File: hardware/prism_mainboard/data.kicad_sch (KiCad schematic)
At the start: 0 parts

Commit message: Mainboard Updates
Started a lot of the basic schematic nets like GND and Power nets. Major Change: Decided on using the XC7Z015-1CLG485I instead of the 7010 or 7020 due to the ability to use HDMI interfaces with an adapter and more LUTs. Updated schematic symbols and footprints accordingly. Added Memory, Encoder, MicroSD schematics. Added LimeSDR footprints as well. Will Try to add Power to the entire board next.
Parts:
- added IC1, IC2: KTDM2G3C618BGCEAT, BGA96C80P9X16_750X1300X100, symbol SamacSys:KTDM2G3C618BGCEAT

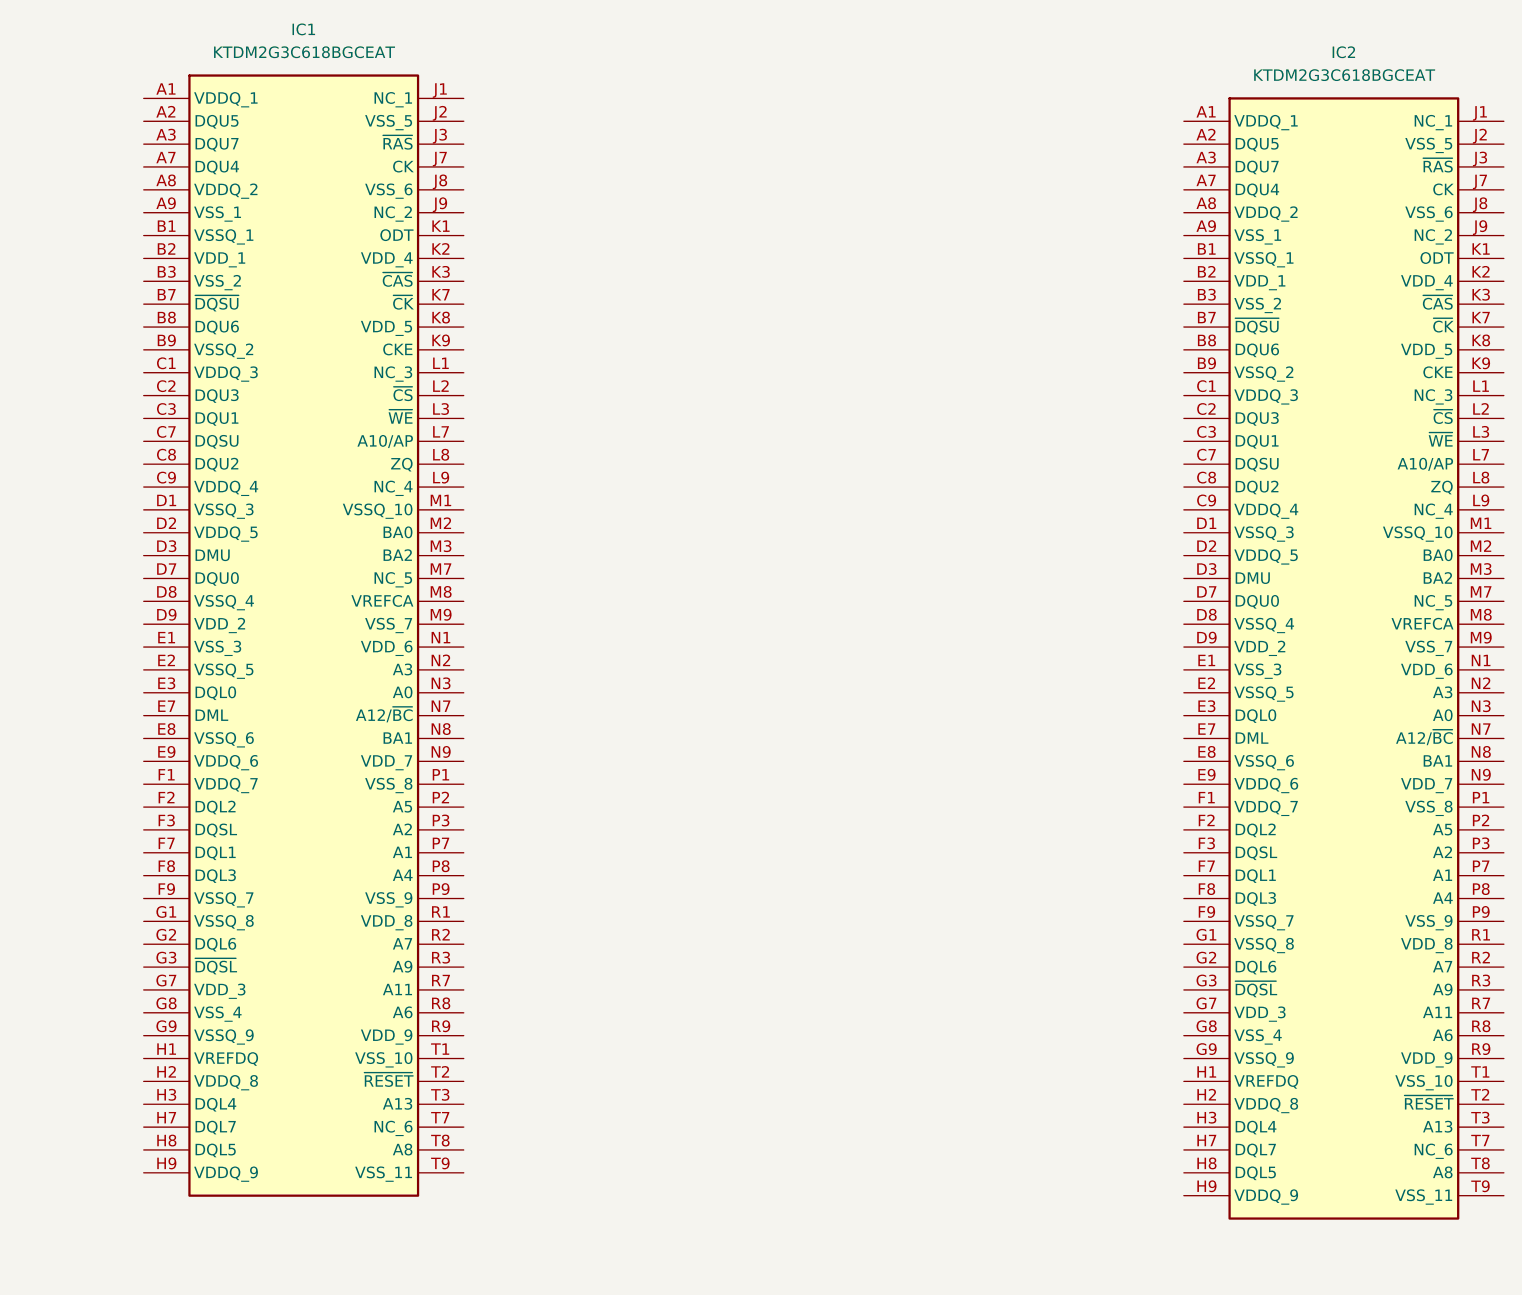
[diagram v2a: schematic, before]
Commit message: Schematic Updates
Updated the DDR3 DRAM to 4Gb, added a lot of nets and started updating the power and decoupling components. Updated .gitignore to avoid .mkv files.
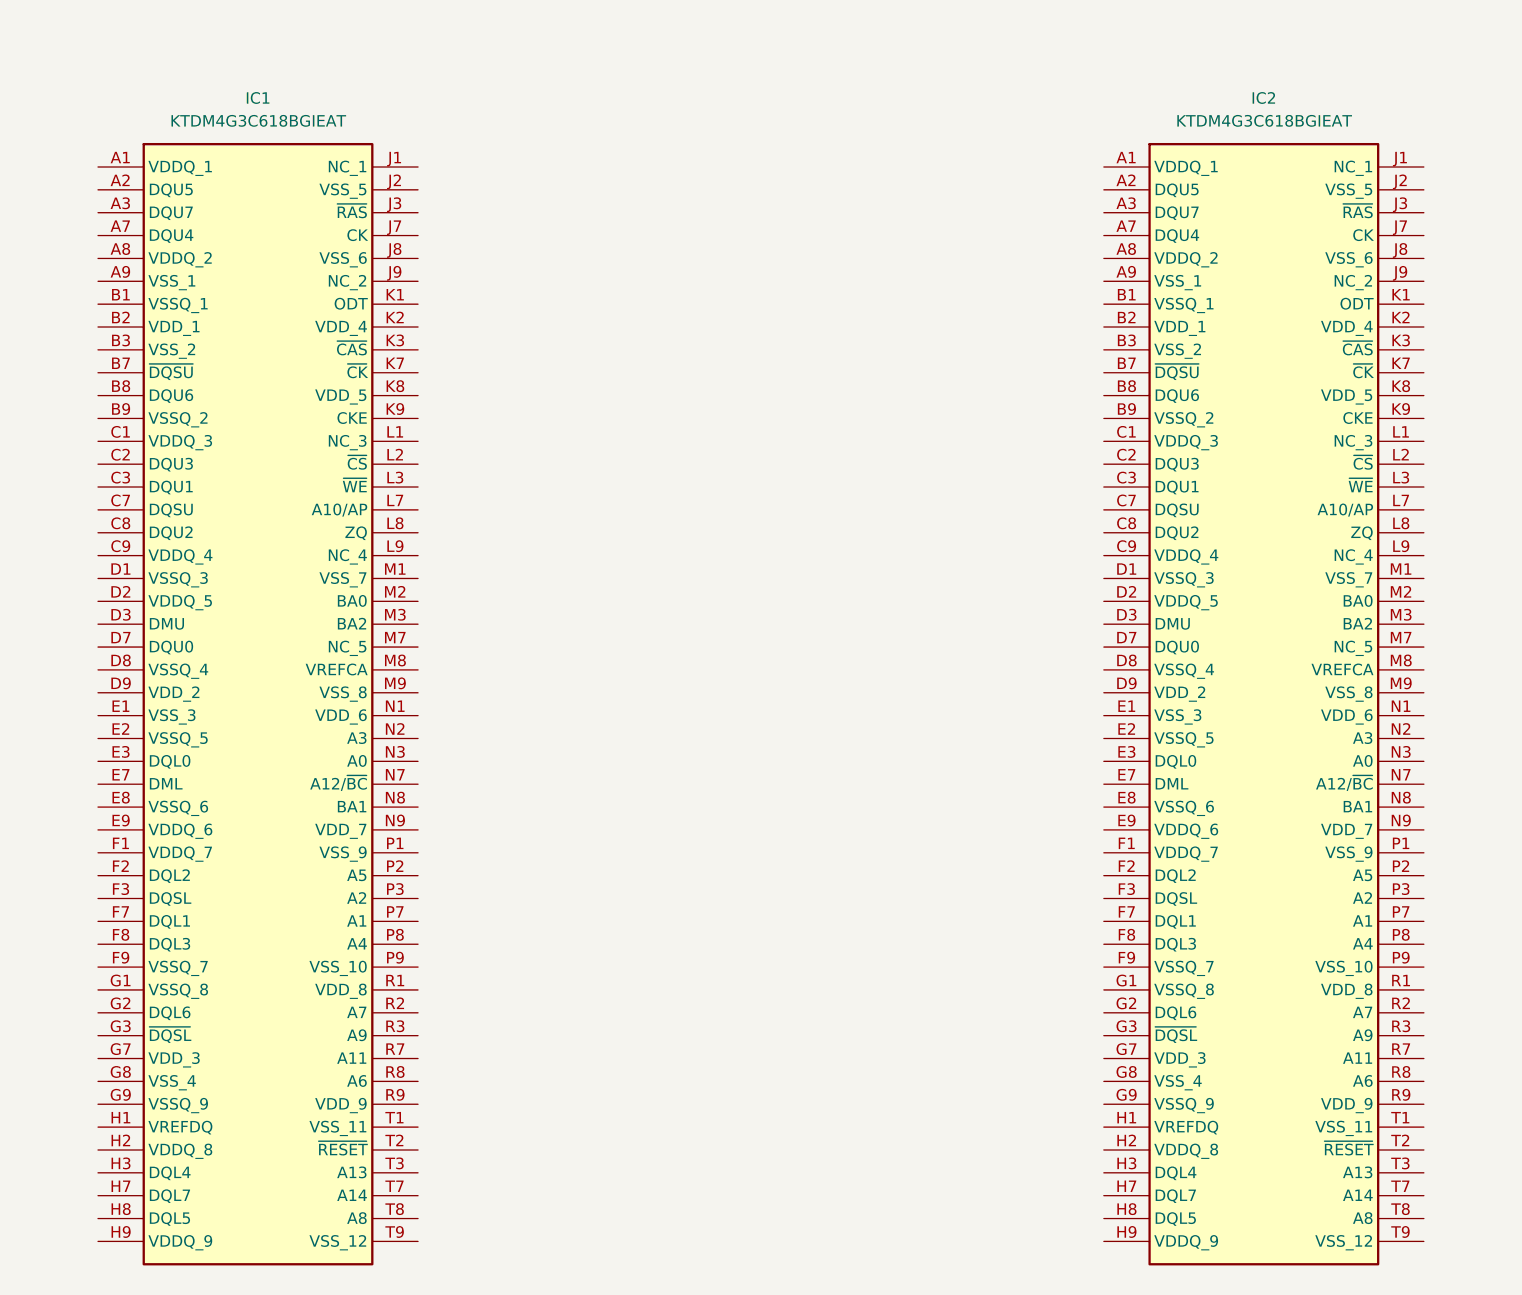
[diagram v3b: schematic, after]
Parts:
- removed IC1, IC2: KTDM2G3C618BGCEAT, BGA96C80P9X16_750X1300X100, symbol SamacSys:KTDM2G3C618BGCEAT
- added IC1, IC2: KTDM4G3C618BGIEAT, BGA96C80P9X16_750X1300X100, symbol SamacSys:KTDM4G3C618BGIEAT

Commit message: Schematic Updates
Updated schematics. Most of the power and decoupling is set for most if not all devices. Need to interconnect devices. Still reading datasheets
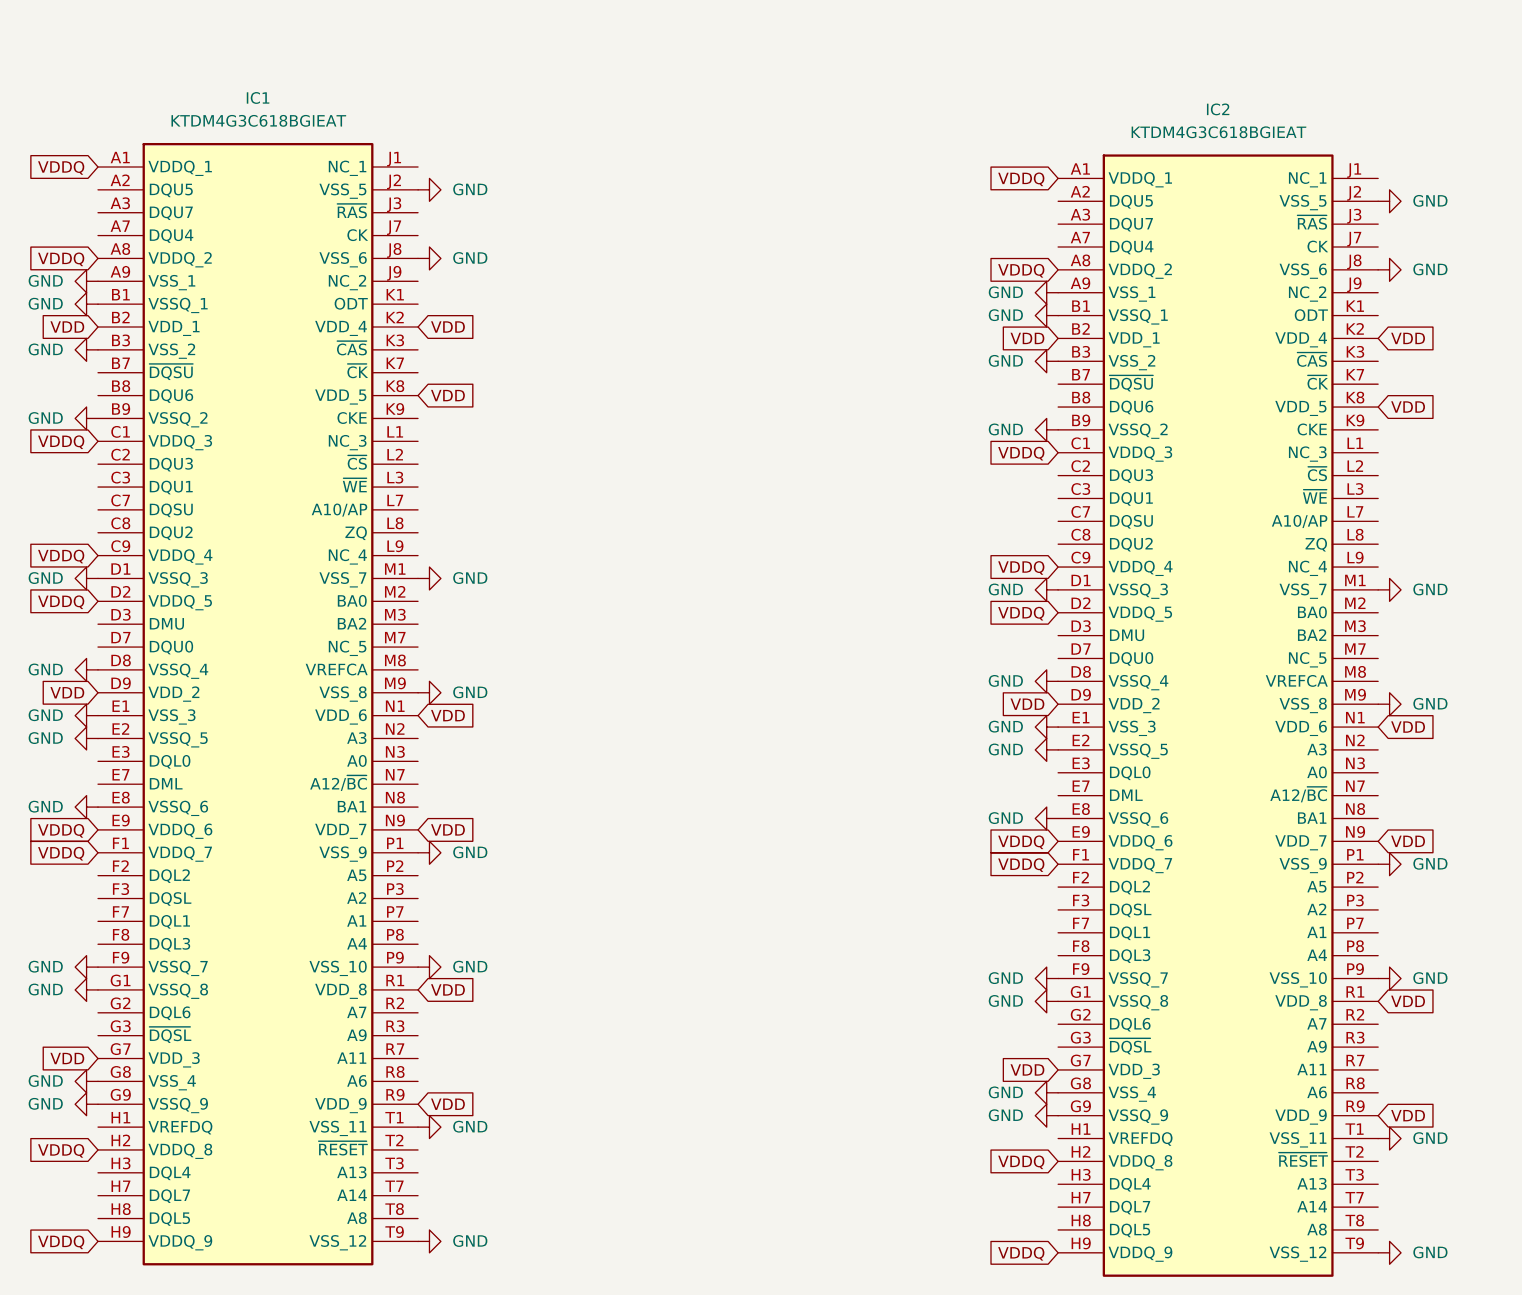
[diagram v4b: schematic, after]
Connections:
- net VDDQ: now reaches IC1.A1 (VDDQ_1)
- net VDDQ: now also IC1.A8 (VDDQ_2), IC1.C1 (VDDQ_3), IC1.C9 (VDDQ_4), IC1.D2 (VDDQ_5), IC1.E9 (VDDQ_6), IC1.F1 (VDDQ_7), IC1.H2 (VDDQ_8), IC1.H9 (VDDQ_9), IC2.A1 (VDDQ_1), IC2.A8 (VDDQ_2), IC2.C1 (VDDQ_3), IC2.C9 (VDDQ_4), IC2.D2 (VDDQ_5), IC2.E9 (VDDQ_6), IC2.F1 (VDDQ_7), IC2.H2 (VDDQ_8), IC2.H9 (VDDQ_9)
- net GND: now reaches IC1.A9 (VSS_1)
- net GND: now also IC1.B1 (VSSQ_1), IC1.B3 (VSS_2), IC1.B9 (VSSQ_2), IC1.D1 (VSSQ_3), IC1.D8 (VSSQ_4), IC1.E1 (VSS_3), IC1.E2 (VSSQ_5), IC1.E8 (VSSQ_6), IC1.F9 (VSSQ_7), IC1.G1 (VSSQ_8), IC1.G8 (VSS_4), IC1.G9 (VSSQ_9), IC1.J2 (VSS_5), IC1.J8 (VSS_6), IC1.M1 (VSS_7), IC1.M9 (VSS_8), IC1.P1 (VSS_9), IC1.P9 (VSS_10), IC1.T1 (VSS_11), IC1.T9 (VSS_12), IC2.A9 (VSS_1), IC2.B1 (VSSQ_1), IC2.B3 (VSS_2), IC2.B9 (VSSQ_2), IC2.D1 (VSSQ_3), IC2.D8 (VSSQ_4), IC2.E1 (VSS_3), IC2.E2 (VSSQ_5), IC2.E8 (VSSQ_6), IC2.F9 (VSSQ_7), IC2.G1 (VSSQ_8), IC2.G8 (VSS_4), IC2.G9 (VSSQ_9), IC2.J2 (VSS_5), IC2.J8 (VSS_6), IC2.M1 (VSS_7), IC2.M9 (VSS_8), IC2.P1 (VSS_9), IC2.P9 (VSS_10), IC2.T1 (VSS_11), IC2.T9 (VSS_12)
- net VDD: now reaches IC1.B2 (VDD_1)
- net VDD: now also IC1.D9 (VDD_2), IC1.G7 (VDD_3), IC1.K2 (VDD_4), IC1.K8 (VDD_5), IC1.N1 (VDD_6), IC1.N9 (VDD_7), IC1.R1 (VDD_8), IC1.R9 (VDD_9), IC2.B2 (VDD_1), IC2.D9 (VDD_2), IC2.G7 (VDD_3), IC2.K2 (VDD_4), IC2.K8 (VDD_5), IC2.N1 (VDD_6), IC2.N9 (VDD_7), IC2.R1 (VDD_8), IC2.R9 (VDD_9)
